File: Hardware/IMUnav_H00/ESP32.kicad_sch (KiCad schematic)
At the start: 19 parts, among them U18 ESP32-C3-MINI-1

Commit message: Added sheets for memory and UserInterface
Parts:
- removed D?: B5819W, Diode_SMD:D_SOD-123, symbol Device:D_Schottky
- U18: LCSC (none) -> C2838502
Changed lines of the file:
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@@
-    (stroke (width 0) (type default))
-  )
-  (wire (pts (xy 132.08 125.73) (xy 132.08 118.11))
     (stroke (width 0) (type default))
   )
@@
   )
   (wire (pts (xy 209.55 26.67) (xy 209.55 104.14))
-    (stroke (width 0) (type default))
-  )
-  (wire (pts (xy 132.08 139.7) (xy 132.08 133.35))
     (stroke (width 0) (type default))
   )
@@
       (project "PaLampa_MoBo_H01"
         (path "/68867493-9f89-4388-916e-56f5ada0ac5c/4ec8e228-d742-4cd8-8c0d-36879b06f45c"
-          (reference "#PWR?") (unit 1)
-        )
-      )
-    )
-  )
-  (symbol (lib_id "power:+3V3") (at 132.08 118.11 0) (unit 1)
-    (in_bom yes) (on_board yes) (dnp no)
-    (property "Reference" "#PWR?" (at 132.08 121.92 0)
-      (effects (font (size 1.27 1.27)) hide)
-    )
-    (property "Value" "+3V3" (at 132.461 113.7158 0)
-      (effects (font (size 1.27 1.27)))
-    )
-    (property "Footprint" "" (at 132.08 118.11 0)
-      (effects (font (size 1.27 1.27)) hide)
-    )
-    (property "Datasheet" "" (at 132.08 118.11 0)
-      (effects (font (size 1.27 1.27)) hide)
-    )
-    (pin "1")
-    (instances
-      (project "IMUnav_H00"
-        (path "/4c2dd95e-3649-4040-ab57-00df6d22e0b0"
-          (reference "#PWR?") (unit 1)
-        )
-        (path "/4c2dd95e-3649-4040-ab57-00df6d22e0b0/bf35eb2a-37f7-4f5f-b34e-af3028cdd96b"
-          (reference "#PWR013") (unit 1)
-        )
-      )
-      (project "PaLampa_MoBo_H01"
-        (path "/68867493-9f89-4388-916e-56f5ada0ac5c"
           (reference "#PWR?") (unit 1)
         )
@@
     )
     (property "Datasheet" "https://www.espressif.com/sites/default/files/documentation/esp32-c3-mini-1_datasheet_en.pdf" (at 171.45 160.02 0)
+      (effects (font (size 1.27 1.27)) hide)
+    )
+    (property "LCSC" "C2838502" (at 171.45 121.92 0)
       (effects (font (size 1.27 1.27)) hide)
     )
@@
     )
   )
-  (symbol (lib_id "power:GND") (at 132.08 139.7 0) (unit 1)
-    (in_bom yes) (on_board yes) (dnp no)
-    (property "Reference" "#PWR?" (at 132.08 146.05 0)
-      (effects (font (size 1.27 1.27)) hide)
-    )
-    (property "Value" "GND" (at 132.207 144.0942 0)
-      (effects (font (size 1.27 1.27)))
-    )
-    (property "Footprint" "" (at 132.08 139.7 0)
-      (effects (font (size 1.27 1.27)) hide)
-    )
-    (property "Datasheet" "" (at 132.08 139.7 0)
-      (effects (font (size 1.27 1.27)) hide)
-    )
-    (pin "1")
-    (instances
-      (project "IMUnav_H00"
-        (path "/4c2dd95e-3649-4040-ab57-00df6d22e0b0"
-          (reference "#PWR?") (unit 1)
-        )
-        (path "/4c2dd95e-3649-4040-ab57-00df6d22e0b0/bf35eb2a-37f7-4f5f-b34e-af3028cdd96b"
-          (reference "#PWR014") (unit 1)
-        )
-      )
-      (project "PaLampa_MoBo_H01"
-        (path "/68867493-9f89-4388-916e-56f5ada0ac5c"
-          (reference "#PWR?") (unit 1)
-        )
-      )
-    )
-  )
   (symbol (lib_id "Device:C") (at 73.66 30.48 0) (unit 1)
     (in_bom yes) (on_board yes) (dnp no)
@@
         )
       )
-    )
-  )
-  (symbol (lib_id "Device:D_Schottky") (at 132.08 129.54 270) (unit 1)
-    (in_bom yes) (on_board yes) (dnp no)
-    (property "Reference" "D?" (at 134.112 128.3716 90)
-      (effects (font (size 1.27 1.27)) (justify left))
-    )
-    (property "Value" "B5819W" (at 134.112 130.683 90)
-      (effects (font (size 1.27 1.27)) (justify left))
-    )
-    (property "Footprint" "Diode_SMD:D_SOD-123" (at 132.08 129.54 0)
-      (effects (font (size 1.27 1.27)) hide)
-    )
-    (property "Datasheet" "~" (at 132.08 129.54 0)
-      (effects (font (size 1.27 1.27)) hide)
-    )
-    (property "LCSC" "C8598" (at 132.08 129.54 90)
-      (effects (font (size 1.27 1.27)) hide)
-    )
-    (pin "1")
-    (pin "2")
-    (instances
-      (project "IMUnav_H00"
-        (path "/4c2dd95e-3649-4040-ab57-00df6d22e0b0"
-          (reference "D?") (unit 1)
-        )
-        (path "/4c2dd95e-3649-4040-ab57-00df6d22e0b0/bf35eb2a-37f7-4f5f-b34e-af3028cdd96b"
-          (reference "D2") (unit 1)
-        )
-      )
-      (project "PaLampa_MoBo_H01"
-        (path "/68867493-9f89-4388-916e-56f5ada0ac5c"
-          (reference "D?") (unit 1)
-        )
-      )

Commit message: Added signal connections to MCU+misc
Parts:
- renumbered U18 to U10
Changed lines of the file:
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@@
         )
         (path "/4c2dd95e-3649-4040-ab57-00df6d22e0b0/bf35eb2a-37f7-4f5f-b34e-af3028cdd96b"
-          (reference "#PWR019") (unit 1)
+          (reference "#PWR0133") (unit 1)
         )
       )
@@
         )
         (path "/4c2dd95e-3649-4040-ab57-00df6d22e0b0/bf35eb2a-37f7-4f5f-b34e-af3028cdd96b"
-          (reference "#PWR0163") (unit 1)
+          (reference "#PWR0134") (unit 1)
         )
       )
@@
         )
         (path "/4c2dd95e-3649-4040-ab57-00df6d22e0b0/bf35eb2a-37f7-4f5f-b34e-af3028cdd96b"
-          (reference "#PWR017") (unit 1)
+          (reference "#PWR0128") (unit 1)
         )
       )
@@
         )
         (path "/4c2dd95e-3649-4040-ab57-00df6d22e0b0/bf35eb2a-37f7-4f5f-b34e-af3028cdd96b"
-          (reference "R2") (unit 1)
+          (reference "R42") (unit 1)
         )
       )
@@
         )
         (path "/4c2dd95e-3649-4040-ab57-00df6d22e0b0/bf35eb2a-37f7-4f5f-b34e-af3028cdd96b"
-          (reference "#PWR021") (unit 1)
+          (reference "#PWR0124") (unit 1)
         )
       )
@@
         )
         (path "/4c2dd95e-3649-4040-ab57-00df6d22e0b0/bf35eb2a-37f7-4f5f-b34e-af3028cdd96b"
-          (reference "R34") (unit 1)
+          (reference "R39") (unit 1)
         )
       )
@@
         )
         (path "/4c2dd95e-3649-4040-ab57-00df6d22e0b0/bf35eb2a-37f7-4f5f-b34e-af3028cdd96b"
-          (reference "#PWR022") (unit 1)
+          (reference "#PWR0131") (unit 1)
         )
       )
@@
         )
         (path "/4c2dd95e-3649-4040-ab57-00df6d22e0b0/bf35eb2a-37f7-4f5f-b34e-af3028cdd96b"
-          (reference "R5") (unit 1)
+          (reference "R45") (unit 1)
         )
       )
@@
         )
         (path "/4c2dd95e-3649-4040-ab57-00df6d22e0b0/bf35eb2a-37f7-4f5f-b34e-af3028cdd96b"
-          (reference "C3") (unit 1)
+          (reference "C39") (unit 1)
         )
       )
@@
   (symbol (lib_id "PCM_Espressif:ESP32-C3-MINI-1") (at 171.45 121.92 0) (unit 1)
     (in_bom yes) (on_board yes) (dnp no) (fields_autoplaced)
-    (property "Reference" "U18" (at 173.6441 92.5027 0)
+    (property "Reference" "U10" (at 173.6441 92.5027 0)
       (effects (font (size 1.27 1.27)) (justify left))
     )
@@
       (project "IMUnav_H00"
         (path "/4c2dd95e-3649-4040-ab57-00df6d22e0b0/bf35eb2a-37f7-4f5f-b34e-af3028cdd96b"
-          (reference "U18") (unit 1)
+          (reference "U10") (unit 1)
         )
       )
@@
         )
         (path "/4c2dd95e-3649-4040-ab57-00df6d22e0b0/bf35eb2a-37f7-4f5f-b34e-af3028cdd96b"
-          (reference "R35") (unit 1)
+          (reference "R40") (unit 1)
         )
       )
@@
         )
         (path "/4c2dd95e-3649-4040-ab57-00df6d22e0b0/bf35eb2a-37f7-4f5f-b34e-af3028cdd96b"
-          (reference "R4") (unit 1)
+          (reference "R44") (unit 1)
         )
       )
@@
         )
         (path "/4c2dd95e-3649-4040-ab57-00df6d22e0b0/bf35eb2a-37f7-4f5f-b34e-af3028cdd96b"
-          (reference "R3") (unit 1)
+          (reference "R43") (unit 1)
         )
       )
@@
         )
         (path "/4c2dd95e-3649-4040-ab57-00df6d22e0b0/bf35eb2a-37f7-4f5f-b34e-af3028cdd96b"
-          (reference "C4") (unit 1)
+          (reference "C41") (unit 1)
         )
       )
@@
         )
         (path "/4c2dd95e-3649-4040-ab57-00df6d22e0b0/bf35eb2a-37f7-4f5f-b34e-af3028cdd96b"
-          (reference "#PWR020") (unit 1)
+          (reference "#PWR0122") (unit 1)
         )
       )
@@
         )
         (path "/4c2dd95e-3649-4040-ab57-00df6d22e0b0/bf35eb2a-37f7-4f5f-b34e-af3028cdd96b"
-          (reference "#PWR016") (unit 1)
+          (reference "#PWR0127") (unit 1)
         )
       )
@@
         )
         (path "/4c2dd95e-3649-4040-ab57-00df6d22e0b0/bf35eb2a-37f7-4f5f-b34e-af3028cdd96b"
-          (reference "#PWR018") (unit 1)
+          (reference "#PWR0132") (unit 1)
         )
       )
@@
         )
         (path "/4c2dd95e-3649-4040-ab57-00df6d22e0b0/bf35eb2a-37f7-4f5f-b34e-af3028cdd96b"
-          (reference "#PWR09") (unit 1)
+          (reference "#PWR0125") (unit 1)
         )
       )
@@
         )
         (path "/4c2dd95e-3649-4040-ab57-00df6d22e0b0/bf35eb2a-37f7-4f5f-b34e-af3028cdd96b"
-          (reference "U3") (unit 1)
+          (reference "U9") (unit 1)
         )
       )
@@
         )
         (path "/4c2dd95e-3649-4040-ab57-00df6d22e0b0/bf35eb2a-37f7-4f5f-b34e-af3028cdd96b"
-          (reference "R1") (unit 1)
+          (reference "R41") (unit 1)
         )
       )
@@
         )
         (path "/4c2dd95e-3649-4040-ab57-00df6d22e0b0/bf35eb2a-37f7-4f5f-b34e-af3028cdd96b"
-          (reference "C6") (unit 1)
+          (reference "C37") (unit 1)
         )
       )
@@
         )
         (path "/4c2dd95e-3649-4040-ab57-00df6d22e0b0/bf35eb2a-37f7-4f5f-b34e-af3028cdd96b"
-          (reference "#PWR011") (unit 1)
+          (reference "#PWR0129") (unit 1)
         )
       )
@@
         )
         (path "/4c2dd95e-3649-4040-ab57-00df6d22e0b0/bf35eb2a-37f7-4f5f-b34e-af3028cdd96b"
-          (reference "#PWR015") (unit 1)
+          (reference "#PWR0123") (unit 1)
         )
       )
@@
         )
         (path "/4c2dd95e-3649-4040-ab57-00df6d22e0b0/bf35eb2a-37f7-4f5f-b34e-af3028cdd96b"
-          (reference "C7") (unit 1)
+          (reference "C38") (unit 1)
         )
       )
@@
         )
         (path "/4c2dd95e-3649-4040-ab57-00df6d22e0b0/bf35eb2a-37f7-4f5f-b34e-af3028cdd96b"
-          (reference "#PWR012") (unit 1)
+          (reference "#PWR0130") (unit 1)
         )
       )
@@
         )
         (path "/4c2dd95e-3649-4040-ab57-00df6d22e0b0/bf35eb2a-37f7-4f5f-b34e-af3028cdd96b"
-          (reference "#PWR010") (unit 1)
+          (reference "#PWR0126") (unit 1)
         )
       )
@@
         )
         (path "/4c2dd95e-3649-4040-ab57-00df6d22e0b0/bf35eb2a-37f7-4f5f-b34e-af3028cdd96b"
-          (reference "C5") (unit 1)
-        )
-      )
+          (reference "C40") (unit 1)
+        )
+      )

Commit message: Semi-final PCB routing (copper only)
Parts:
- C?: footprint Capacitor_SMD:C_0603_1608Metric -> Capacitor_SMD:C_0805_2012Metric; LCSC C19702 -> C15850
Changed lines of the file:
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@@
       (effects (font (size 1.27 1.27)) (justify left))
     )
-    (property "Footprint" "Capacitor_SMD:C_0603_1608Metric" (at 74.6252 34.29 0)
+    (property "Footprint" "Capacitor_SMD:C_0805_2012Metric" (at 74.6252 34.29 0)
       (effects (font (size 1.27 1.27)) hide)
     )
@@
       (effects (font (size 1.27 1.27)) hide)
     )
-    (property "LCSC" "C19702" (at 73.66 30.48 0)
+    (property "LCSC" "C15850" (at 73.66 30.48 0)
       (effects (font (size 1.27 1.27)) hide)
     )

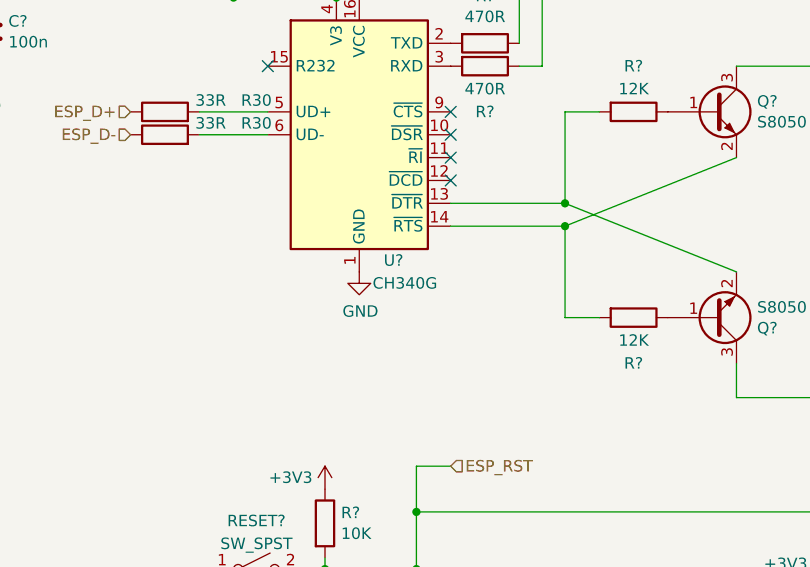
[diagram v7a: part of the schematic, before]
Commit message: PCB touch-ups, bom file for testing
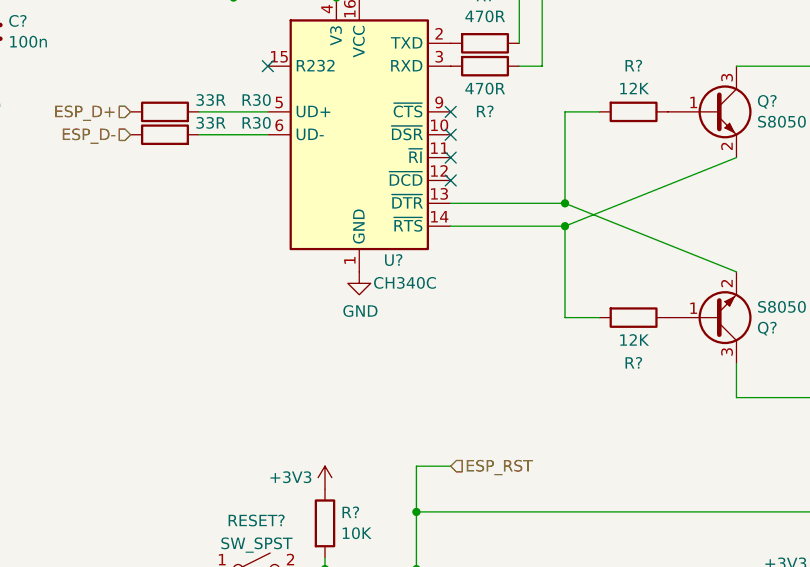
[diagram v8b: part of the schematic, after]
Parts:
- U?: value CH340G -> CH340C
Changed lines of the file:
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@@
       (effects (font (size 1.27 1.27)))
     )
-    (property "Value" "CH340G" (at 129.54 58.42 0)
+    (property "Value" "CH340C" (at 129.54 58.42 0)
       (effects (font (size 1.27 1.27)))
     )
